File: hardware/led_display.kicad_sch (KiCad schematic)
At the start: 12 parts, among them U1 MAX6952, U2 MAX6952

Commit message: Assign footprints
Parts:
- C1, C2, C3, C4, C5, C6: footprint (none) -> Capacitor_SMD:C_0805_2012Metric
- R1, R3, R4, R5: footprint (none) -> Resistor_SMD:R_0805_2012Metric
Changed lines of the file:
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@@
       (effects (font (size 1.27 1.27)) (justify right))
     )
-    (property "Footprint" "" (at 78.232 125.73 90)
+    (property "Footprint" "Resistor_SMD:R_0805_2012Metric" (at 78.232 125.73 90)
       (effects (font (size 1.27 1.27)) hide)
     )
@@
       (effects (font (size 1.27 1.27)) (justify right))
     )
-    (property "Footprint" "" (at 224.028 125.73 90)
+    (property "Footprint" "Resistor_SMD:R_0805_2012Metric" (at 224.028 125.73 90)
       (effects (font (size 1.27 1.27)) hide)
     )
@@
       (effects (font (size 1.27 1.27)) (justify right))
     )
-    (property "Footprint" "" (at 223.2152 140.97 0)
+    (property "Footprint" "Capacitor_SMD:C_0805_2012Metric" (at 223.2152 140.97 0)
       (effects (font (size 1.27 1.27)) hide)
     )
@@
       (effects (font (size 0.762 0.762)) (justify left))
     )
-    (property "Footprint" "" (at 101.6 60.96 0)
+    (property "Footprint" "Capacitor_SMD:C_0805_2012Metric" (at 101.6 60.96 0)
       (effects (font (size 1.27 1.27)) hide)
     )
@@
       (effects (font (size 0.762 0.762)) (justify left))
     )
-    (property "Footprint" "" (at 91.44 60.96 0)
+    (property "Footprint" "Capacitor_SMD:C_0805_2012Metric" (at 91.44 60.96 0)
       (effects (font (size 1.27 1.27)) hide)
     )
@@
       (effects (font (size 0.762 0.762)) (justify left))
     )
-    (property "Footprint" "" (at 200.66 60.96 0)
+    (property "Footprint" "Capacitor_SMD:C_0805_2012Metric" (at 200.66 60.96 0)
       (effects (font (size 1.27 1.27)) hide)
     )
@@
       (effects (font (size 0.762 0.762)) (justify left))
     )
-    (property "Footprint" "" (at 210.82 60.96 0)
+    (property "Footprint" "Capacitor_SMD:C_0805_2012Metric" (at 210.82 60.96 0)
       (effects (font (size 1.27 1.27)) hide)
     )
@@
       (effects (font (size 1.27 1.27)) (justify right))
     )
-    (property "Footprint" "" (at 225.298 109.22 90)
+    (property "Footprint" "Resistor_SMD:R_0805_2012Metric" (at 225.298 109.22 90)
       (effects (font (size 1.27 1.27)) hide)
     )
@@
       (effects (font (size 1.27 1.27)) (justify right))
     )
-    (property "Footprint" "" (at 79.0448 140.97 0)
+    (property "Footprint" "Capacitor_SMD:C_0805_2012Metric" (at 79.0448 140.97 0)
       (effects (font (size 1.27 1.27)) hide)
     )
@@
       (effects (font (size 1.27 1.27)) (justify right))
     )
-    (property "Footprint" "" (at 78.232 109.22 90)
-      (effects (font (size 1.27 1.27)) hide)
-    )
+    (property "Footprint" "Resistor_SMD:R_0805_2012Metric" (at 78.232 109.22 90)
+      (effects (font (size 1.27 1.27)) hide)
+    )

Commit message: Starting PCB routing process
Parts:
- R4: value 4.7k -> R

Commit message: Routing in progress
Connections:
- net +3.3V_LED: now reaches C3.1, C6.1, U2.32 (V+), U2.33 (V+)
- net +3.3V_LED: now also C2.1, C5.1, R3.1, R4.1, U1.32 (V+), U1.33 (V+)
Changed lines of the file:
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@@
 			)
 		)
-		(property "Description" "Power symbol creates a global label with name \"+3.3V\""
+		(property "Description" "Power symbol creates a global label with name \"PWR_LED\""
 			(at 81.28 100.33 0)
 			(effects
@@
 		(dnp no)
 		(fields_autoplaced yes)
-		(property "Reference" "#PWR0218"
+		(property "Reference" "#PWR_LED0218"
 			(at 95.25 60.96 0)
 			(effects
@@
 			)
 		)
-		(property "Description" "Power symbol creates a global label with name \"+3.3V\""
+		(property "Description" "Power symbol creates a global label with name \"PWR_LED\""
 			(at 95.25 57.15 0)
 			(effects
@@
 			(project "broadcast_clock"
 				(path "/40ecfd14-7e3d-4342-87f4-c464dfcd4cdf/425f15d8-7995-473a-916f-1acbbdb328a4/80bf7467-8bed-48f3-ab7b-174979e1b2eb"
-					(reference "#PWR0218")
+					(reference "#PWR_LED0218")
 					(unit 1)
 				)
@@
 		(dnp no)
 		(fields_autoplaced yes)
-		(property "Reference" "#PWR0220"
+		(property "Reference" "#PWR_LED0220"
 			(at 204.47 60.96 0)
 			(effects
@@
 			)
 		)
-		(property "Description" "Power symbol creates a global label with name \"+3.3V\""
+		(property "Description" "Power symbol creates a global label with name \"PWR_LED\""
 			(at 204.47 57.15 0)
 			(effects
@@
 			(project "broadcast_clock"
 				(path "/40ecfd14-7e3d-4342-87f4-c464dfcd4cdf/425f15d8-7995-473a-916f-1acbbdb328a4/80bf7467-8bed-48f3-ab7b-174979e1b2eb"
-					(reference "#PWR0220")
+					(reference "#PWR_LED0220")
 					(unit 1)
 				)
@@
 		(on_board yes)
 		(dnp no)
-		(property "Reference" "#PWR050"
+		(property "Reference" "#PWR_LED050"
 			(at 223.52 106.68 0)
 			(effects
@@
 			)
 		)
-		(property "Description" "Power symbol creates a global label with name \"+3.3V\""
+		(property "Description" "Power symbol creates a global label with name \"PWR_LED\""
 			(at 223.52 102.87 0)
 			(effects
@@
 			(project "broadcast_clock"
 				(path "/40ecfd14-7e3d-4342-87f4-c464dfcd4cdf/425f15d8-7995-473a-916f-1acbbdb328a4/80bf7467-8bed-48f3-ab7b-174979e1b2eb"
-					(reference "#PWR050")
-					(unit 1)
-				)
+					(reference "#PWR_LED050")
+					(unit 1)
+				)

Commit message: Prototype, starting on firmware
Former-commit-id: 3c22e4f94bda4a4eed472ac1ff762e7709731c05
Former-commit-id: afce4fecf5b4961621dea2f3a514203675ae8e80
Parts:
- R4: value R -> 4.7k
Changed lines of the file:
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@@
 			)
 		)
-		(property "Value" "R"
+		(property "Value" "4.7k"
 			(at 78.74 107.9499 0)
 			(effects

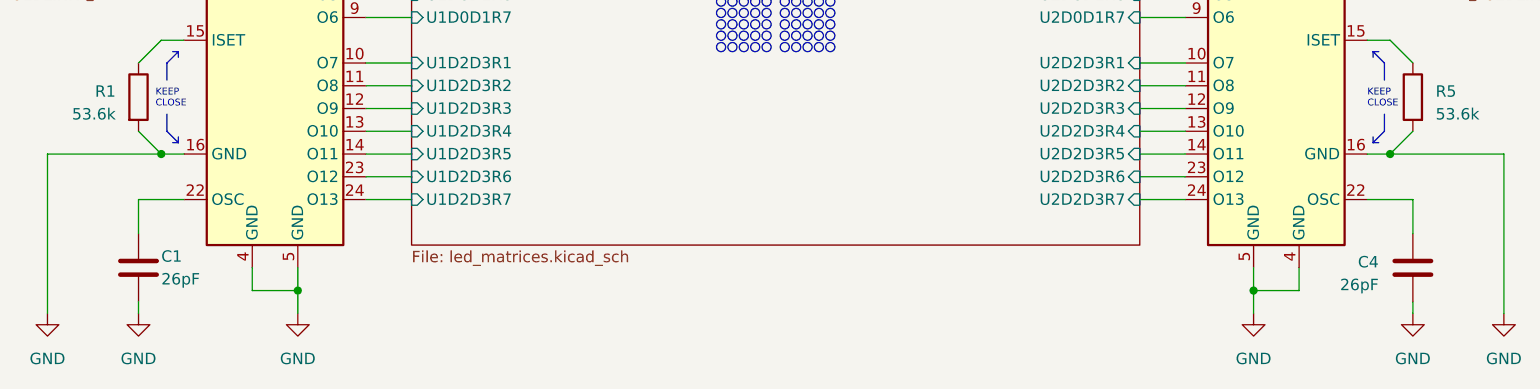
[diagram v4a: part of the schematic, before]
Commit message: Change capacitor value from 26 to 27 pF which is a standard value
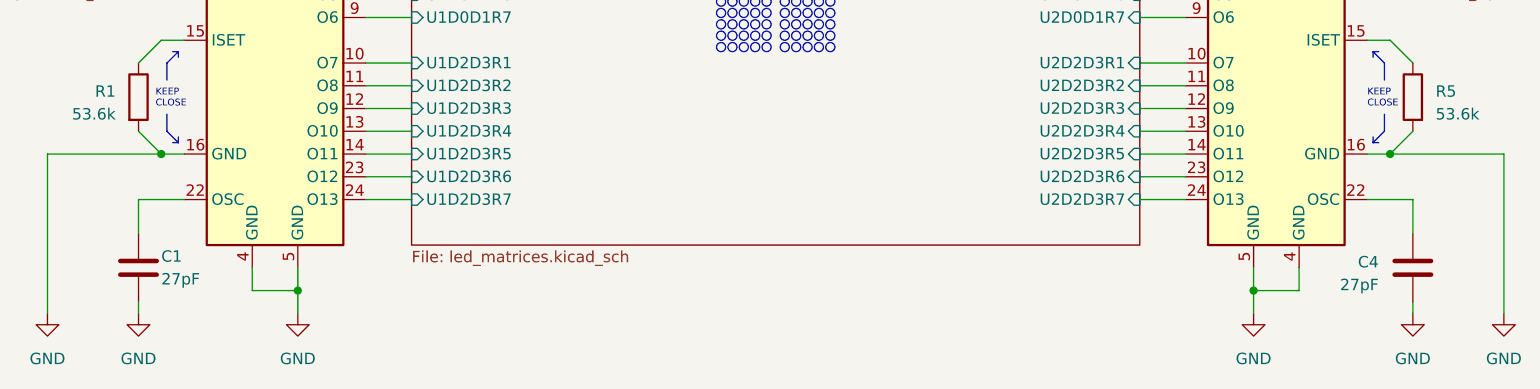
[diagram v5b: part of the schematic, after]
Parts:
- C1, C4: value 26pF -> 27pF
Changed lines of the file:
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@@
 			)
 		)
-		(property "Value" "26pF"
+		(property "Value" "27pF"
 			(at 218.44 146.685 0)
 			(effects
@@
 			)
 		)
-		(property "Value" "26pF"
+		(property "Value" "27pF"
 			(at 82.55 146.05 0)
 			(effects

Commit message: Minor design updates
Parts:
- C5, C6: value 47uF -> 47µF
- R1, R5: value 53.6k -> 53,6kΩ
- R3, R4: value 4.7k -> 4,7kΩ
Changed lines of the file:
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@@
 			)
 		)
-		(property "Value" "53.6k"
+		(property "Value" "53,6kΩ"
 			(at 77.47 127.635 0)
 			(effects
@@
 			)
 		)
-		(property "Value" "53.6k"
+		(property "Value" "53,6kΩ"
 			(at 224.79 127.635 0)
 			(effects
@@
 			)
 		)
-		(property "Value" "47uF"
+		(property "Value" "47µF"
 			(at 105.41 59.69 0)
 			(effects
@@
 			)
 		)
-		(property "Value" "47uF"
+		(property "Value" "47µF"
 			(at 214.63 59.69 0)
 			(effects
@@
 			)
 		)
-		(property "Value" "4.7k"
+		(property "Value" "4,7kΩ"
 			(at 226.06 111.125 0)
 			(effects
@@
 			)
 		)
-		(property "Value" "4.7k"
+		(property "Value" "4,7kΩ"
 			(at 78.74 107.9499 0)
 			(effects
